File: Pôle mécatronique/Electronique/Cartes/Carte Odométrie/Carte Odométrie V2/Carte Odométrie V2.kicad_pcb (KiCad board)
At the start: 2 copper layers, 49.5 x 58.4 mm, 8 parts

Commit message: Update Carte Odométrie
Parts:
- removed BUSCAN+ALIM: Conn_01x04, Connector_JST:JST_PH_B4B-PH-K_1x04_P2.00mm_Vertical
- removed CAN_Transceiver1: TCAN332, empreinte:SO-8_S
- removed Lidar: Conn_01x05, Connector_JST:JST_PH_B5B-PH-K_1x05_P2.00mm_Vertical
- removed STM32 f303k8: NUCLEO-F303K8, empreinte:MODULE_NUCLEO-F303K8
- added A1: NUCLEO-F303K8, empreinte:MODULE_NUCLEO-F303K8, B.Cu at (149.9, 101.6)
- added G***: LOGO, Logos:logoRobotechNancy10x10, B.Cu at (160.2, 70.4)
- added J1: Conn_01x08, Connector_PinSocket_2.54mm:PinSocket_1x08_P2.54mm_Vertical, B.Cu at (158.1, 133.3)
- added J2: Conn_01x05, Connector_JST:JST_PH_B5B-PH-K_1x05_P2.00mm_Vertical, B.Cu at (165.7, 86.4)
- added J3: Conn_01x04, Connector_JST:JST_PH_B4B-PH-K_1x04_P2.00mm_Vertical, B.Cu at (132.1, 85.7)
- added J4: Conn_01x07, Connector_JST:JST_PH_B7B-PH-K_1x07_P2.00mm_Vertical, B.Cu at (129.6, 114.7)
- added J5: Conn_01x07, Connector_PinSocket_2.54mm:PinSocket_1x07_P2.54mm_Vertical, B.Cu at (167.6, 101.0)
- added U1: TCAN332, empreinte:SO-8_S, F.Cu at (130.2, 102.9)
- moved REF 13.1 mm to (168.4, 65.7)
- moved REF 12.5 mm to (127.9, 65.7)
- moved REF 7.73 mm to (129.5, 134.6)
- moved REF 7.62 mm to (167.6, 134.6)
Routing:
- net +5V: track 53.7 -> 175.7 mm
- net GND: track 31.6 -> 131.9 mm
- net I2C_SDA: track 0.00 -> 54.5 mm, vias 0 -> 4
- net I2C_SCL: track 0.00 -> 47.9 mm
- net SPI_MISO: track 0.00 -> 31.7 mm
- net SPI_MOSI: track 0.00 -> 30.5 mm
- net SPI_CLK: track 0.00 -> 24.5 mm, vias 0 -> 2
- net CAN_TX: track 0.00 -> 21.0 mm
- net CAN_RX: track 1.24 -> 18.3 mm
- net +BATT: track 9.85 -> 24.9 mm
- net UART1_TX: track 15.4 -> 24.9 mm
- net UART1_RX: track 13.8 -> 22.2 mm
- net CAN_L: track 43.0 -> 46.7 mm, vias 0 -> 2
- net +3V3: track 21.6 -> 24.9 mm
- net CAN_H: track 64.4 -> 65.6 mm, vias 0 -> 2
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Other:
- board size 49.5 x 58.4 mm -> 48.9 x 78.2 mm
- board text added: "I2C_SDA"
- board text added: "I2C_SDL"
- board text added: "ROBOTECH NANCY"
- board text added: "SPI_CLK"
- board text added: "SPI_MISO"
- board text added: "SPI_MOSI"
- board text removed: "3.3V"
- board text removed: "CAN_H"
- board text removed: "CAN_L"

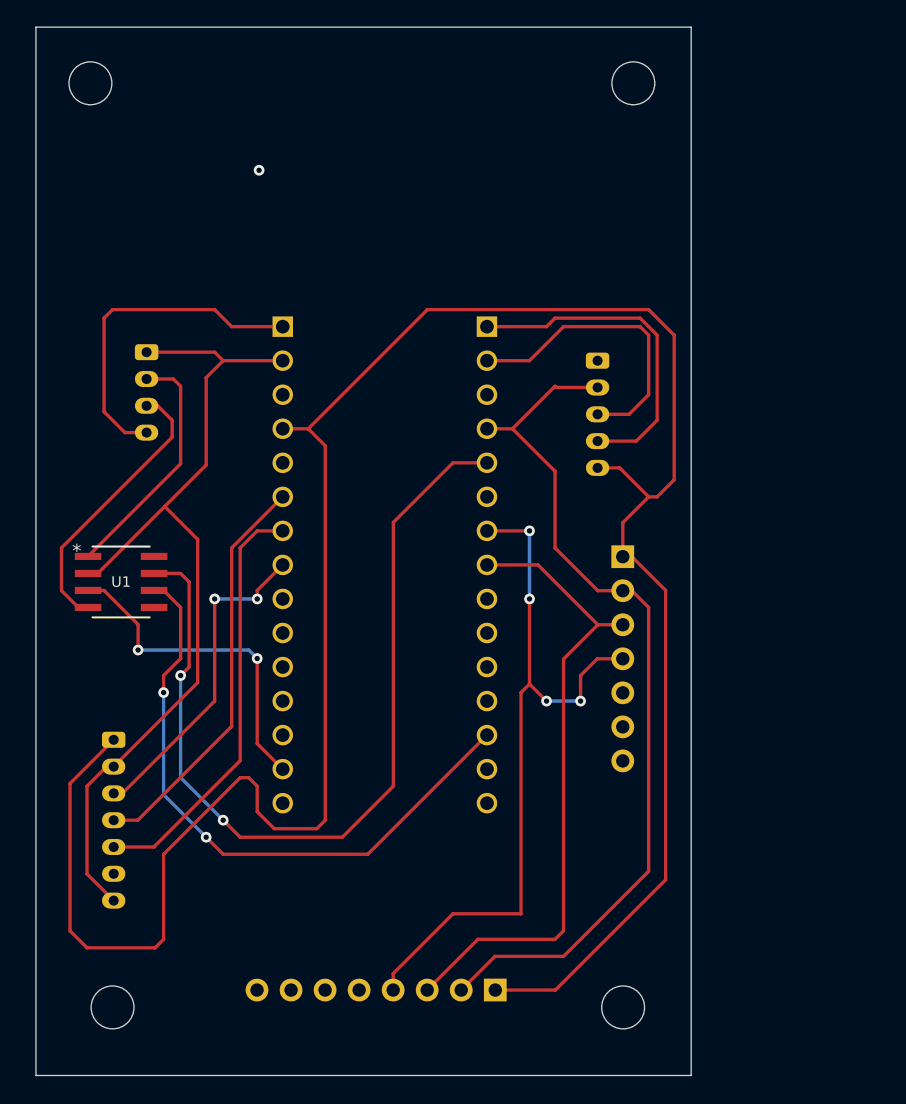
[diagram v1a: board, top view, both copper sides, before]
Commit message: carte odométrie avec resistance pull up
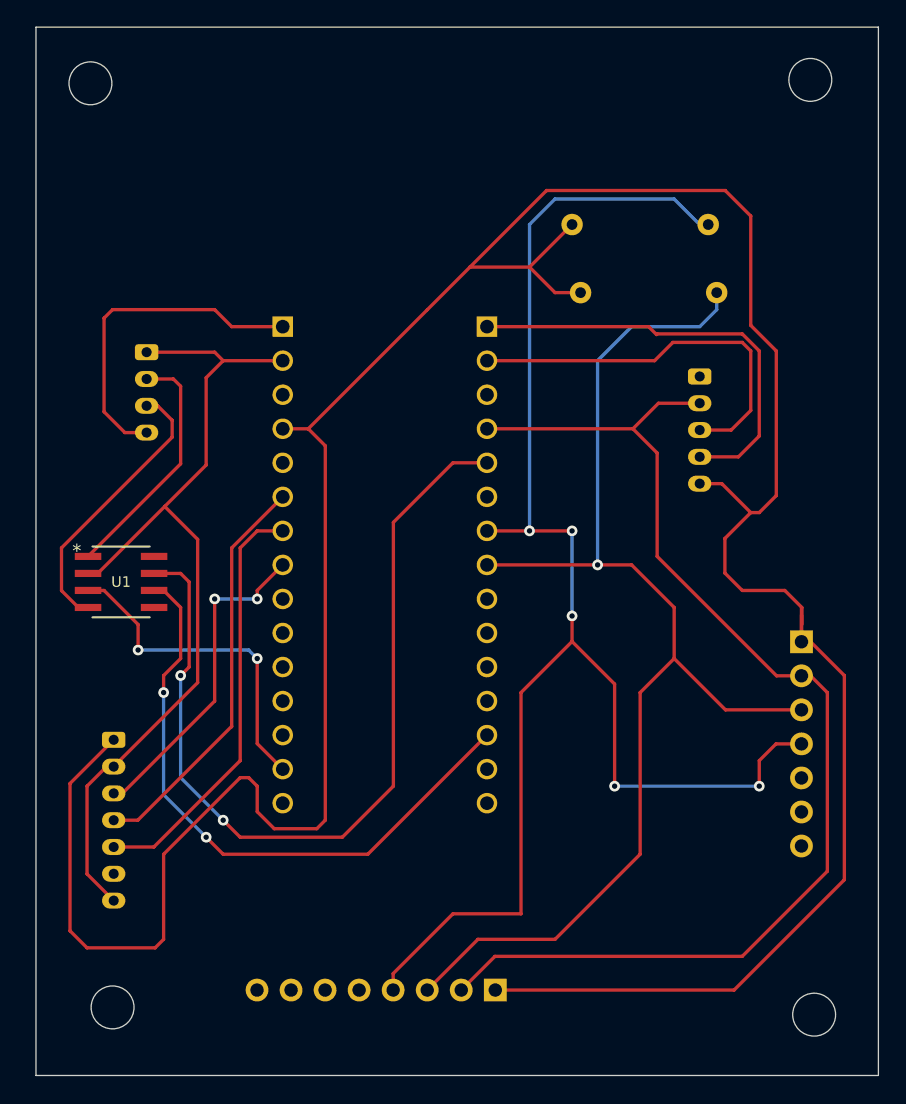
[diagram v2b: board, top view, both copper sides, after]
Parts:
- added R1: 10000ohm, Resistor_THT:R_Axial_DIN0207_L6.3mm_D2.5mm_P10.16mm_Horizontal, B.Cu at (163.8, 76.2)
- added R2: 10000ohm, Resistor_THT:R_Axial_DIN0207_L6.3mm_D2.5mm_P10.16mm_Horizontal, B.Cu at (174.6, 81.3)
- moved J5 14.8 mm to (180.9, 107.3)
- moved REF 14.3 mm to (181.9, 135.2)
- moved REF 13.2 mm to (181.6, 65.4)
- moved G*** 7.78 mm to (167.0, 66.7)
- moved J2 7.71 mm to (173.4, 87.5)
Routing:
- net I2C_SDA: track 54.5 -> 115.6 mm, vias 4 -> 5
- net +5V: track 175.7 -> 228.5 mm
- net I2C_SCL: track 47.9 -> 92.9 mm, vias 0 -> 1
- net GND: track 131.9 -> 154.1 mm
- net UART1_TX: track 24.9 -> 32.5 mm
- net UART1_RX: track 22.2 -> 29.4 mm
- net (no net): vias 1 -> 0
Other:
- board size 48.9 x 78.2 mm -> 62.9 x 78.2 mm

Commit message: Carte odométrie v2 "fini"
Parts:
- moved R1 10.2 mm to (174.0, 76.2), turned to 180 degrees
- moved R2 8.91 mm to (165.7, 80.6), turned to 0 degrees
- moved J4 1.99 mm to (130.3, 112.8)
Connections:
- A1 pad 3.13: CAN_L -> CAN_TX
- A1 pad 3.5: CAN_H -> CAN_RX
- A1 pad 4.9: unconnected-(A1-Pad4.9) -> SPI_CS
- J2 pad 3: UART1_RX -> UART1_TX
- J2 pad 4: UART1_TX -> UART1_RX
- J3 pad 2: CAN_RX -> CAN_H
- J3 pad 3: CAN_TX -> CAN_L
- J4 pad 2: GND -> SPI_CS
- J4 pad 6: unconnected-(J4-Pad6) -> (no net)
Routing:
- net CAN_RX: track 18.3 -> 88.9 mm
- net CAN_H: track 65.6 -> 16.8 mm, vias 2 -> 0
- net CAN_TX: track 21.0 -> 65.3 mm, vias 0 -> 2
- net GND: track 154.1 -> 189.7 mm, vias 0 -> 4
- net CAN_L: track 46.7 -> 15.7 mm, vias 2 -> 0
- net SPI_CS: track 0.00 -> 19.1 mm, vias 0 -> 2
- net I2C_SDA: track 115.6 -> 100.1 mm, vias 5 -> 4
- net UART1_TX: track 32.5 -> 21.2 mm, vias 0 -> 2
- net UART1_RX: track 29.4 -> 20.3 mm, vias 0 -> 2
- net I2C_SCL: track 92.9 -> 86.7 mm, vias 1 -> 0
- net +5V: track 228.5 -> 225.9 mm, vias 0 -> 2
- net +BATT: track 24.9 -> 23.0 mm, vias 0 -> 2
- net SPI_MISO: track 31.7 -> 33.3 mm
- net SPI_CLK: track 24.5 -> 23.8 mm
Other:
- board text added: "SPI_CS"
